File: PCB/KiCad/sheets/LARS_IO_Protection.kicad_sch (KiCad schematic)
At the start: 57 parts, among them U6 SN74S1051DR, U7 SN74S1051DR, U8 SN74S1051DR, U9 SN74S1051DR

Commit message: reannotate schematic
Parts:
- renumbered C58 to C61, C59 to C62, C60 to C63, C61 to C64, R31 to R25, R32 to R26, R26 to R27, R27 to R28, R28 to R31, R25 to R32, R52 to R34, R53 to R35, R54 to R36, R34 to R37, R35 to R38, R40 to R39, R41 to R40, R37 to R41, R36 to R42, R39 to R43, R38 to R44, R42 to R45, R43 to R46, R44 to R47, R45 to R48, R46 to R49, R47 to R50, R48 to R51, R49 to R52, R50 to R53, R51 to R54, R72 to R55, R73 to R56, R71 to R57, R69 to R58, R70 to R59, R55 to R60, R56 to R61, R57 to R62, R58 to R63, R67 to R64, R68 to R65, R61 to R66, R62 to R67, R59 to R68, R60 to R69, R63 to R70, R64 to R71, R65 to R72, R66 to R73

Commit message: add final traces
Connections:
- net GPIO1': now also U6.12 (D09); no longer U6.10 (D07)
- net GPIO3': now also U6.10 (D07); no longer U6.12 (D09)
- net I2C1_IO1': now also U7.13 (D10); no longer U7.15 (D12)
- net I2C1_IO2': now also U7.12 (D09); no longer U7.14 (D11)
- net I2C1_IO3': now also U7.11 (D08); no longer U7.2 (D01)
- net I2C1_IO4': now also U7.10 (D07); no longer U7.3 (D02)
- net I2C1_IO5': now also U7.14 (D11); no longer U7.4 (D03)
- net I2C1_IO6': now also U7.15 (D12); no longer U7.5 (D04)
- net I2C1_IO7': now also U7.3 (D02); no longer U7.6 (D05)
- net I2C1_IO8': now also U7.2 (D01); no longer U7.7 (D06)
- net I2C1_SCL': now also U7.6 (D05); no longer U7.12 (D09)
- net I2C1_SDA': now also U7.7 (D06); no longer U7.11 (D08)
- net I2C2_IO1': now also U9.12 (D09); no longer U9.15 (D12)
- net I2C2_IO2': now also U9.13 (D10); no longer U9.14 (D11)
- net I2C2_IO3': now also U9.14 (D11); no longer U9.13 (D10)
- net I2C2_IO4': now also U9.15 (D12); no longer U9.12 (D09)
- net SPI1_CS1: now also R55.2; no longer R56.2
- net SPI1_CS1': now also R55.1, U8.15 (D12); no longer R56.1, U8.14 (D11)
- net SPI1_CS2: now also R56.2; no longer R55.2
- net SPI1_CS2': now also R56.1, U8.14 (D11); no longer R55.1, U8.15 (D12)
- net UART1_RX: now also R30.2; no longer R29.2
- net UART1_RX': now also R30.1, U6.2 (D01); no longer R29.1, U6.3 (D02)
- net UART1_TX: now also R29.2; no longer R30.2
- net UART1_TX': now also R29.1, U6.3 (D02); no longer R30.1, U6.2 (D01)
- net UART3_RX: now also R26.2; no longer R25.2
- net UART3_TX: now also R25.2; no longer R26.2
- net STM_NRST: now reaches U8.10 (D07)
- no-connect marks 3 -> 2
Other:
- moved on the sheet: R34, R35, R36, R38, R39, R40, R41, R42, R43, R44, R66, R68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

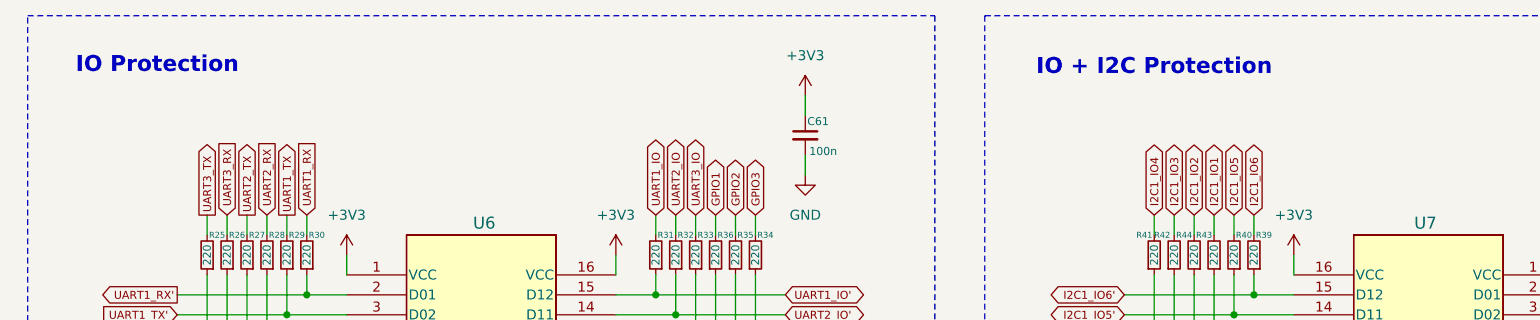
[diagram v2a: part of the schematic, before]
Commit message: change default KiCad schematic font
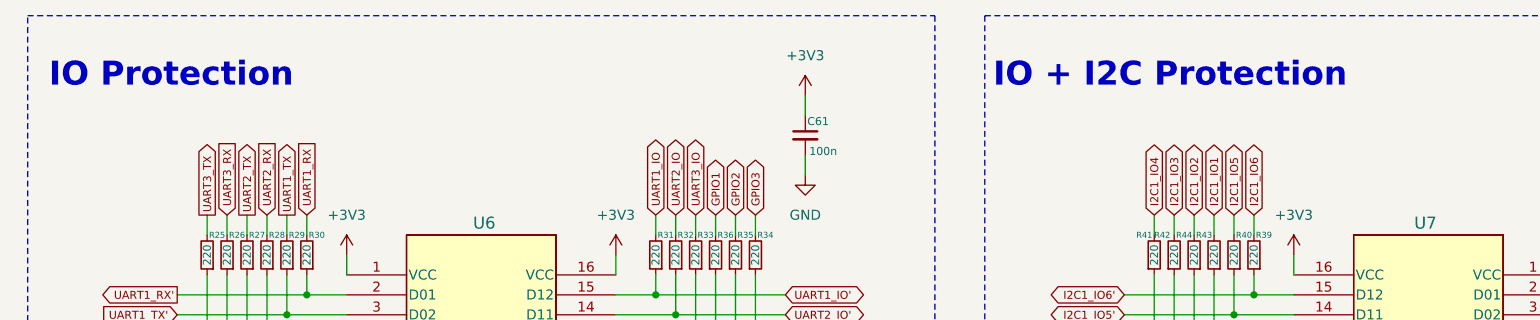
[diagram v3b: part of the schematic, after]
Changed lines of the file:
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@@
 	(text "IO + I2C Protection"
 		(exclude_from_sim no)
-		(at 162.56 25.654 0)
+		(at 164.592 26.67 0)
 		(effects
 			(font
-				(size 2.032 2.032)
+				(size 3.048 3.048)
 				(thickness 0.4064)
 				(bold yes)
@@
 	(text "IO Protection"
 		(exclude_from_sim no)
-		(at 35.56 25.4 0)
+		(at 37.338 26.67 0)
 		(effects
 			(font
-				(size 2.032 2.032)
+				(size 3.048 3.048)
 				(thickness 0.4064)
 				(bold yes)

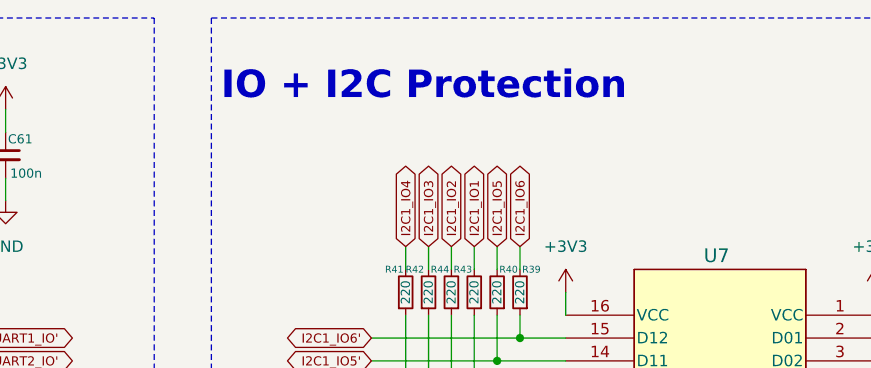
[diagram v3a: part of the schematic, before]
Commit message: update text layout and fix remaining DRC errors
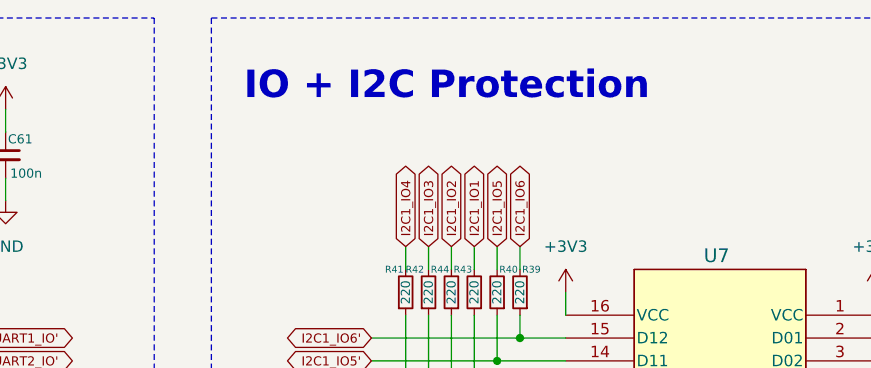
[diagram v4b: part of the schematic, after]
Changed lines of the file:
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@@
 	(text "IO + I2C Protection"
 		(exclude_from_sim no)
-		(at 164.592 26.67 0)
+		(at 167.132 26.67 0)
 		(effects
 			(font

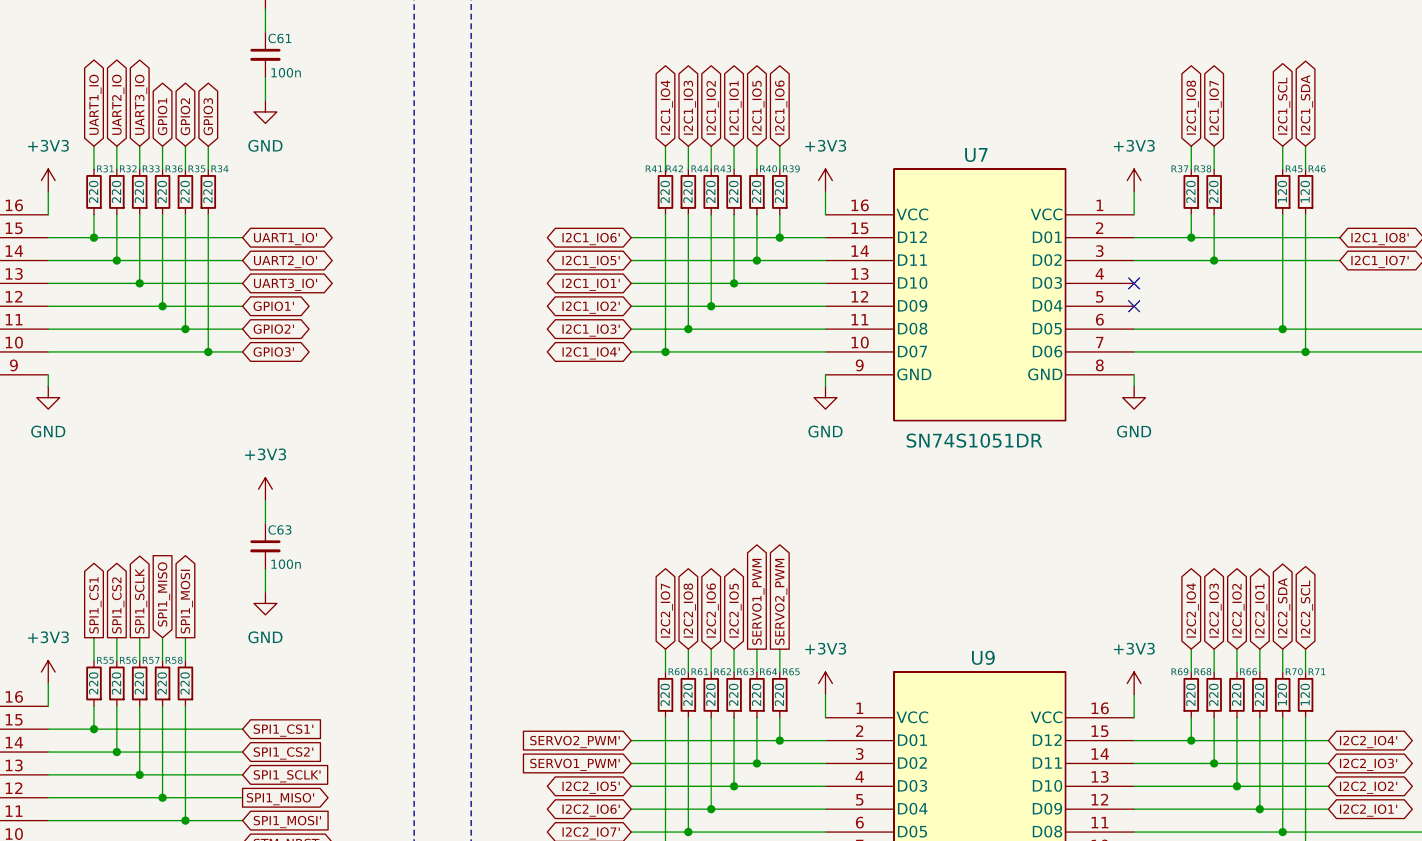
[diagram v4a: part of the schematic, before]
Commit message: add ESD protection and update footprints
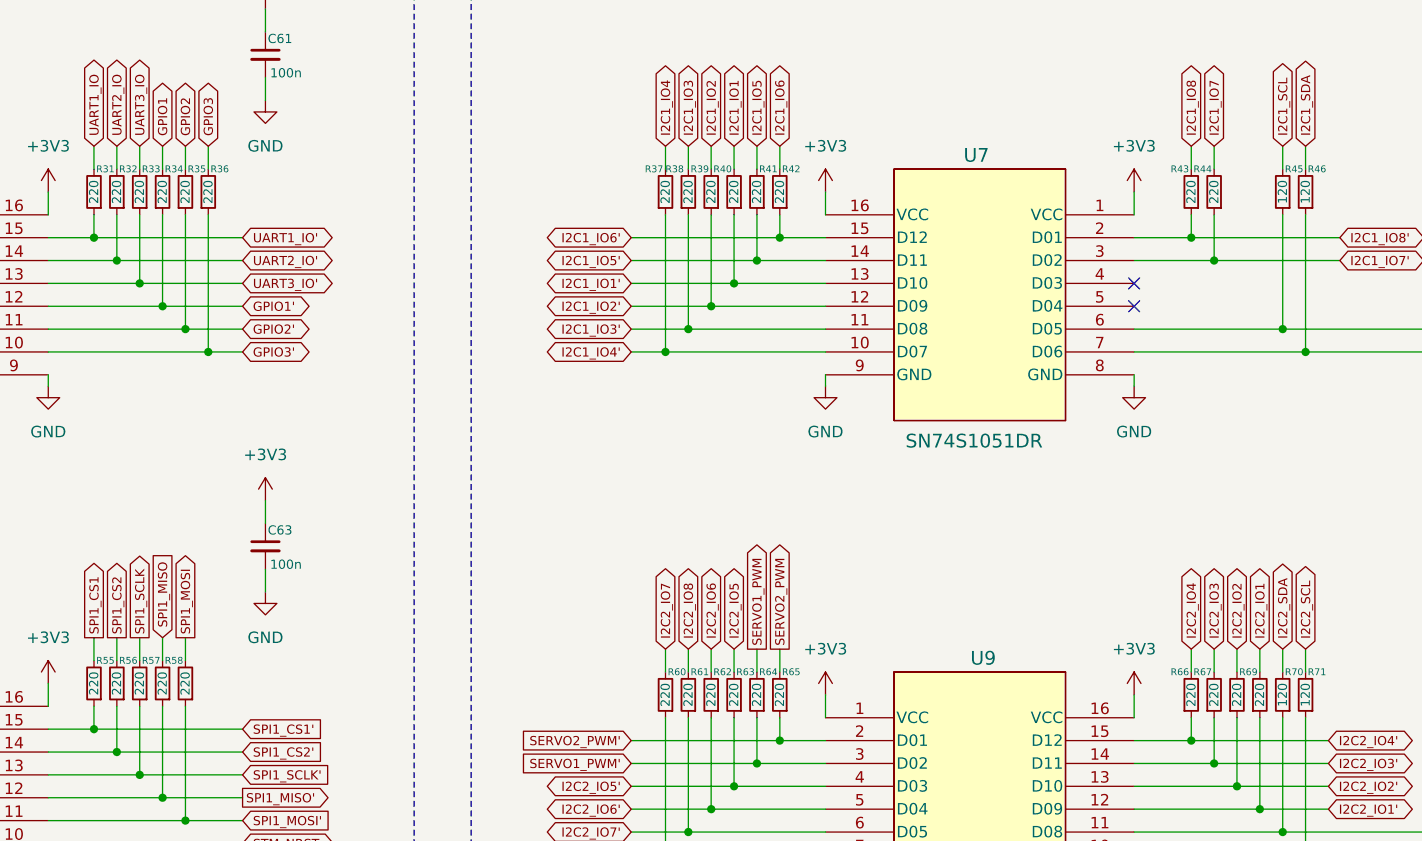
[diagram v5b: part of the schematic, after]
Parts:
- renumbered R36 to R34, R34 to R36, R41 to R37, R42 to R38, R44 to R39, R43 to R40, R40 to R41, R39 to R42, R37 to R43, R38 to R44, R69 to R66, R68 to R67, R67 to R68, R66 to R69

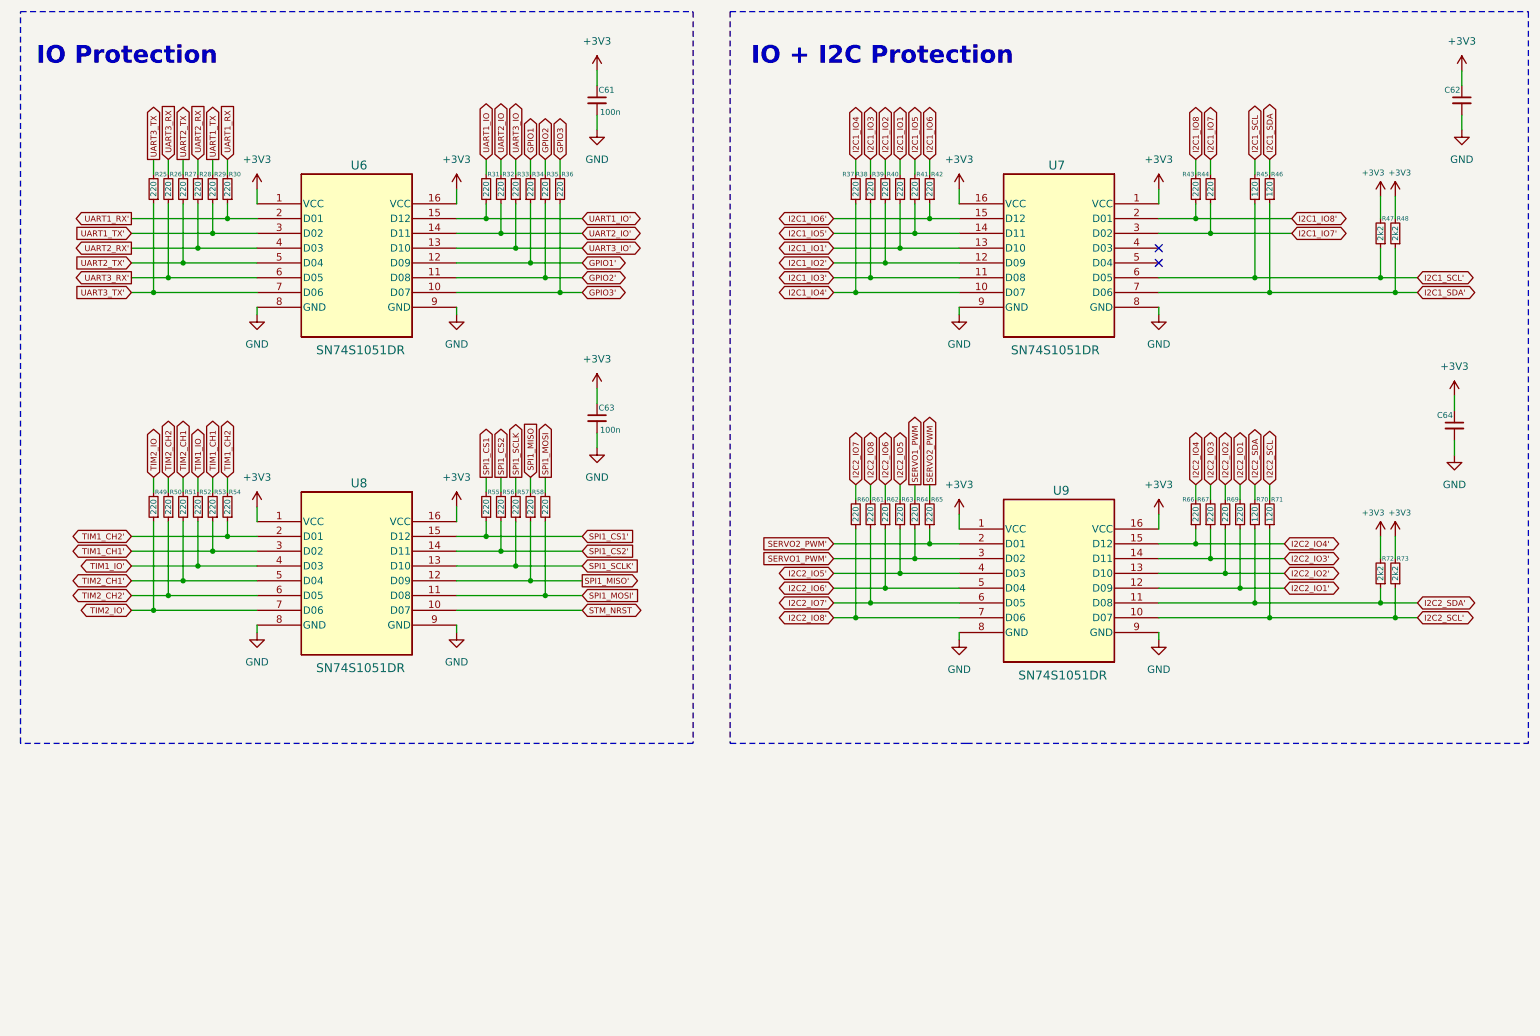
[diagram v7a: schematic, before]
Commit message: PCB: add XOR gate for RC Receiver
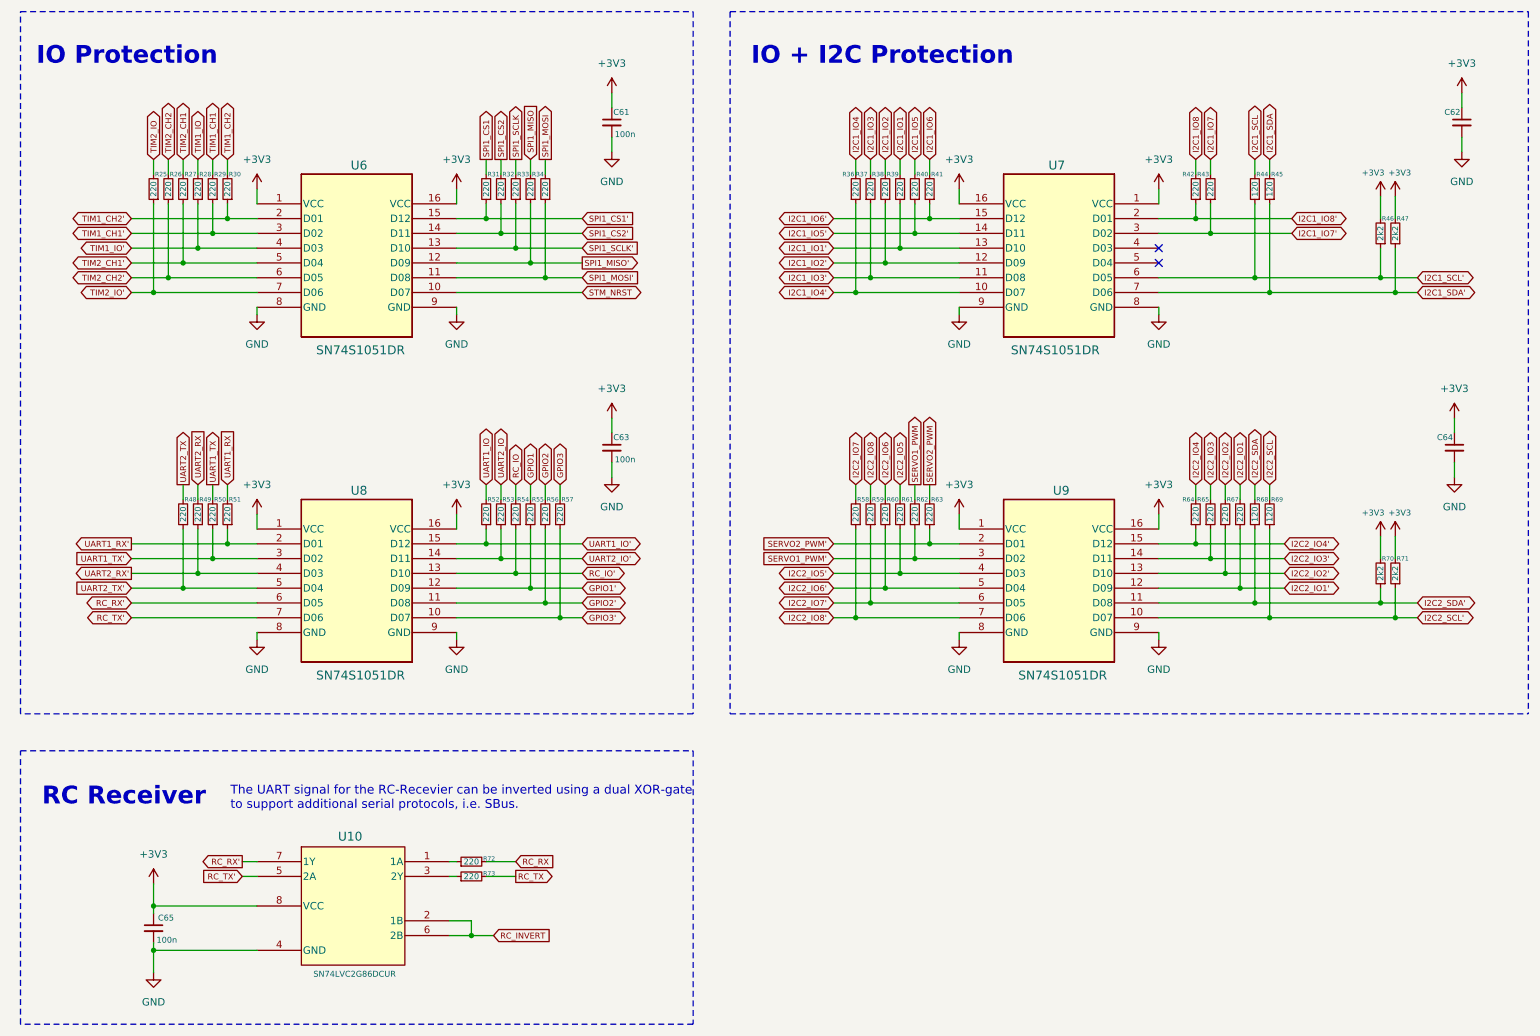
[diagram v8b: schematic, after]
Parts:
- added C65: 100n, LARS_Hardware_Interface:C_0805_2012Metric, symbol LARS_Hardware_Interface:C_Small
- added U10: SN74LVC2G86DCUR, LARS_Hardware_Interface:SN74LVC2G86, symbol LARS_Hardware_Interface:SN74LVC2G86DCUR
- renumbered C63 to C61, C61 to C63, R49 to R25, R50 to R26, R51 to R27, R52 to R28, R53 to R29, R54 to R30, R55 to R31, R56 to R32, R57 to R33, R58 to R34, R59 to R35, R37 to R36, R38 to R37, R39 to R38, R40 to R39, R41 to R40, R42 to R41, R43 to R42, R44 to R43, R45 to R44, R46 to R45, R47 to R46, R48 to R47, R27 to R48, R28 to R49, R29 to R50, R30 to R51, R31 to R52, R32 to R53, R33 to R54, R34 to R55, R35 to R56, R36 to R57, R60 to R58, R61 to R59, R62 to R60, R63 to R61, R64 to R62, R65 to R63, R66 to R64, R67 to R65, R68 to R66, R69 to R67, R70 to R68, R71 to R69, R72 to R70, R73 to R71, R25 to R72, R26 to R73, U8 to U6, U6 to U8
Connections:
- net +3V3: now also C65.1, U10.8 (VCC)
- net GND: now also C65.2, U10.4 (GND)
- net UART3_IO renamed RC_IO
- net UART3_IO' renamed RC_IO'
- net UART3_RX renamed RC_TX
- net UART3_RX': no longer names the net of R73.1
- net UART3_RX': now also U10.3 (2Y); no longer U8.6 (D05)
- net UART3_TX renamed RC_RX
- net UART3_TX': no longer names the net of R72.1
- net UART3_TX': now also U10.1 (1A); no longer U8.7 (D06)
- new net RC_INVERT: U10.2 (1B), U10.6 (2B)
- new net RC_RX': U10.7 (1Y), U8.6 (D05)
- new net RC_TX': U10.5 (2A), U8.7 (D06)
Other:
- note added: "RC Receiver"
- note added: "The UART signal for the RC-Recevier can be inverted using a dual XOR-gate to support additional serial protocols, i.e. SBus."
- moved on the sheet: C61, C62, C63, C64, R25, R26, R27, R28, R29, R30, R31, R32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
